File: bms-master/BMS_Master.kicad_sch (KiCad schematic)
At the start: 79 parts, among them J1 PWR, J2 PROG, J3 BMS_M_OUT, J4 BMS_M_IN, J5 CAN, J6 Current_Sensor, Q1 BC807, SW1 SW_SPST, U1 AP2204K-ADJ, U2 AP2204K-ADJ, U3 STM32F103C8Tx, U4 BQ79600-Q1, U5 SN65HVD256D, Y1 8M, Y2 32.768k

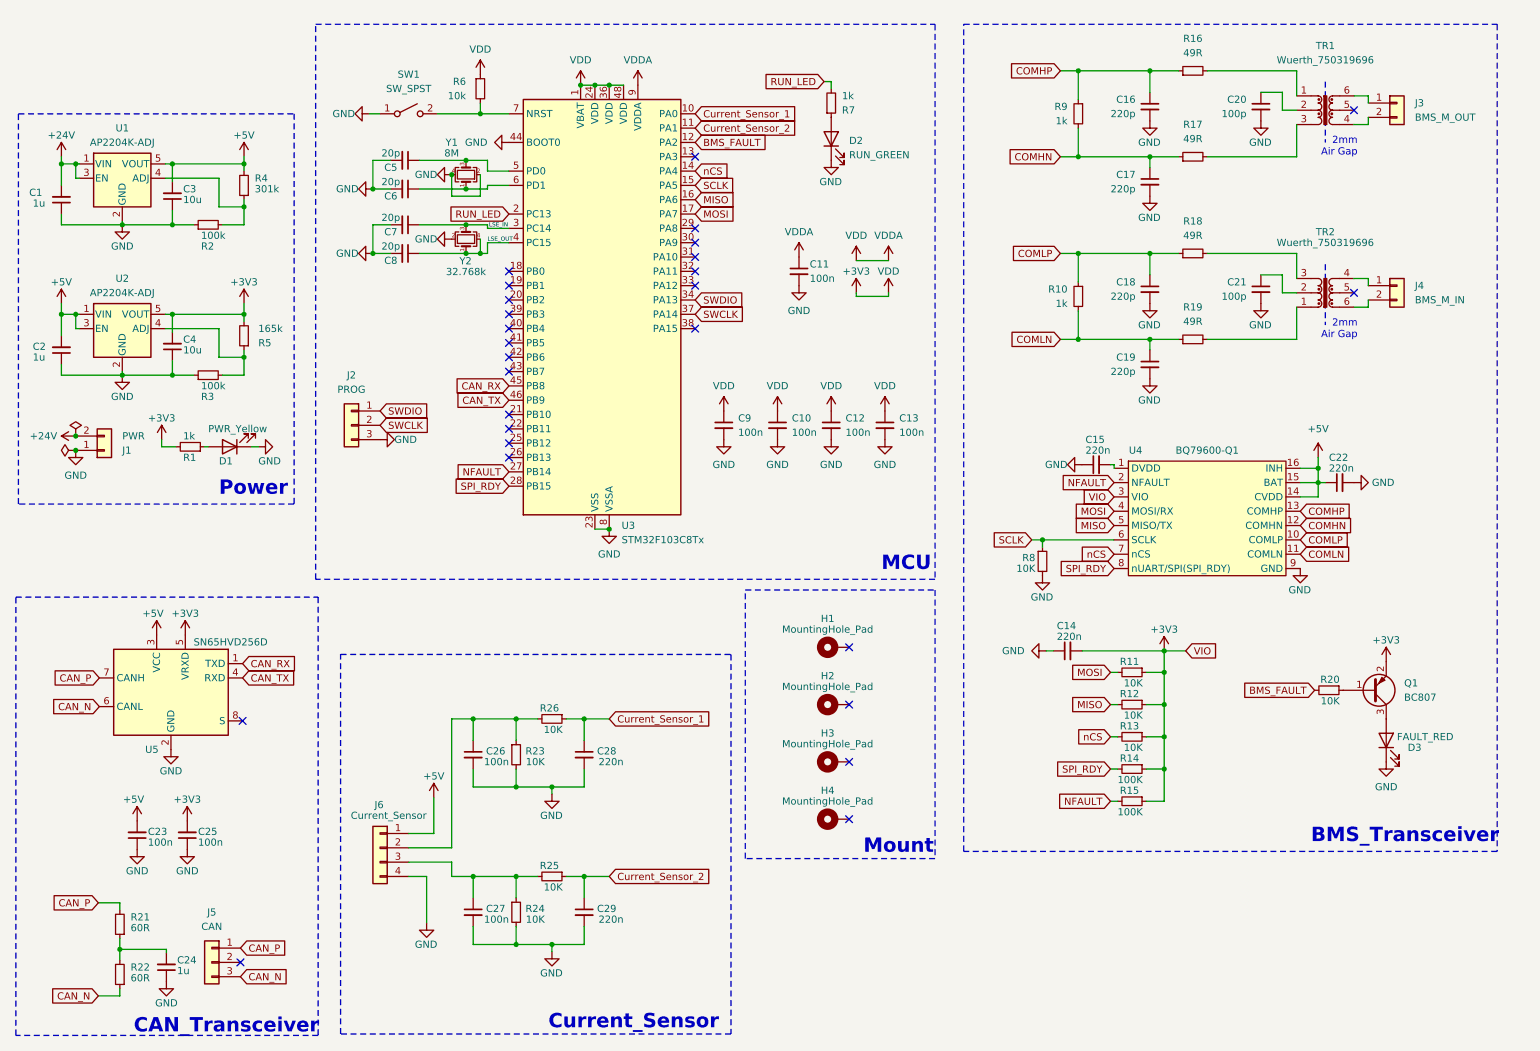
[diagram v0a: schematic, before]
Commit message: feat(bms master): current sensor circuits
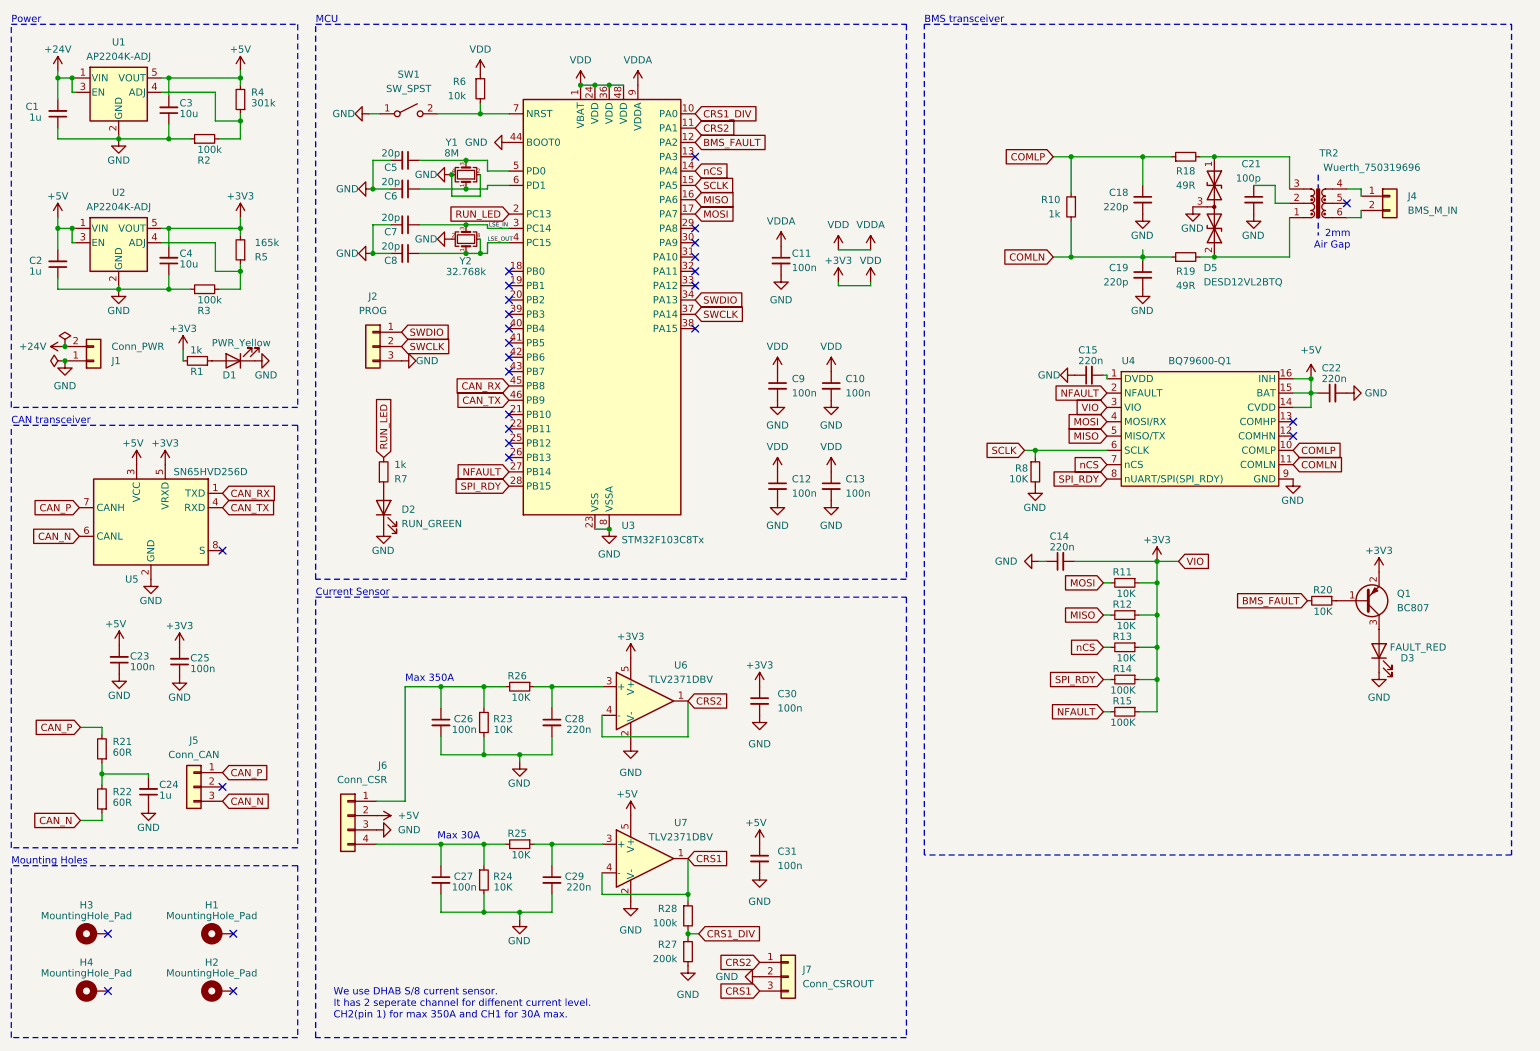
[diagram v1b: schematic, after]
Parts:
- removed C16, C17: 220p, Capacitor_SMD:C_0603_1608Metric, symbol Device:C_Small
- removed C20: 100p, Capacitor_SMD:C_0603_1608Metric, symbol Device:C_Small
- removed J3: BMS_M_OUT, Connector_Molex:Molex_Micro-Fit_3.0_43650-0200_1x02_P3.00mm_Horizontal, symbol Connector_Generic:Conn_01x02
- removed R16, R17: 49R, Resistor_SMD:R_0603_1608Metric, symbol Device:R_Small
- removed R9: 1k, Resistor_SMD:R_0603_1608Metric, symbol Device:R_Small
- removed TR1: Wuerth_750319696, Transformer_SMD:Transformer_Wuerth_750315371, symbol Transformer:Wuerth_750315371
- added C30, C31: 100n, symbol Device:C_Small
- added D5: DESD12VL2BTQ, Package_TO_SOT_SMD:SOT-23, symbol Device:D_TVS_Dual_AAC
- added J7: Conn_CSROUT, symbol Connector_Generic:Conn_01x03
- added R27: 200k, symbol Device:R_Small
- added R28: 100k, symbol Device:R_Small
- added U6, U7: TLV2371DBV, Package_TO_SOT_SMD:SOT-23-5, symbol Amplifier_Operational:TLV2371DBV
- J1: value PWR -> Conn_PWR
- J5: value CAN -> Conn_CAN
- J6: value Current_Sensor -> Conn_CSR
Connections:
- net +3V3: now also C30.1, U6.5 (V+)
- net +5V: now also J6.2 (Pin_2), C31.1, U7.5 (V+); no longer J6.1 (Pin_1)
- net GND: now also J6.3 (Pin_3), C30.2, C31.2, D5.3 (common), J7.2 (Pin_2), R27.2, U6.2 (V-), U7.2 (V-); no longer J6.4 (Pin_4)
- net at R19.2, TR2.1: now also D5.2 (A2)
- net at C26.1, R23.1, R26.2: now also J6.1 (Pin_1); no longer J6.2 (Pin_2)
- net at C27.1, R24.1, R25.2: now also J6.4 (Pin_4); no longer J6.3 (Pin_3)
- net at R18.2, TR2.3: now also D5.1 (A1)
- net COMHN: no longer names the net of U4.12 (COMHN)
- net COMHP: no longer names the net of U4.13 (COMHP)
- net Current_Sensor_1: no longer names the net of C28.1, R26.1
- net Current_Sensor_1: now also U6.3 (+); no longer U3.10 (PA0)
- net Current_Sensor_2: no longer names the net of C29.1, R25.1
- net Current_Sensor_2: now also U7.3 (+); no longer U3.11 (PA1)
- new net CRS1: J7.3 (Pin_3), R28.1, U7.1, U7.4 (-)
- new net CRS1_DIV: R27.1, R28.2, U3.10 (PA0)
- new net CRS2: J7.1 (Pin_1), U3.11 (PA1), U6.1, U6.4 (-)
- no-connect marks 27 -> 28
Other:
- note added: "BMS transceiver"
- note added: "CAN transceiver"
- note added: "Current Sensor"
- note added: "Max 30A"
- note added: "Max 350A"
- note added: "Mounting Holes"
- note added: "We use DHAB S/8 current sensor. It has 2 seperate channel for diffenent current level. CH2(pin 1) for max 350A and CH1 for 30A max."
- note removed: "BMS_Transceiver"
- note removed: "CAN_Transceiver"
- note removed: "Current_Sensor"
- note removed: "Mount"
- company: NCKU Formula SAE -> NCKU Formula Racing
- moved on the sheet: C1, C10, C11, C12, C13, C14, C15, C18, C19, C2, C21, C22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
